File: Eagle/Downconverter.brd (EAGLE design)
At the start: 160 x 100 mm, 25 parts, among them J2 3.5HEADPHONEJACK, J5 U.FL_CONN, J6 U.FL_CONN, U1 5V_REG, U2 MIXER, U3 DUAL_OP_AMP_LMV822, U4 DIGITAL_POTDIGITAL_POT

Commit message: changes to layout
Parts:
- moved C1 1.80 mm to (3.17, 19.1)
- moved U1 1.42 mm to (10.2, 20.3)
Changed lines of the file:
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@@
 </autorouter>
 <elements>
-<element name="C1" library="764Library" package="R0603" package3d_urn="urn:adsk.eagle:package:26057/1" value="10uF" x="4.445" y="17.78" smashed="yes">
-<attribute name="NAME" x="3.81" y="18.415" size="1.27" layer="25"/>
-<attribute name="VALUE" x="2.54" y="15.875" size="1.27" layer="27"/>
+<element name="C1" library="764Library" package="R0603" package3d_urn="urn:adsk.eagle:package:26057/1" value="10uF" x="3.175" y="19.05" smashed="yes">
+<attribute name="NAME" x="1.27" y="16.51" size="1.27" layer="25"/>
+<attribute name="VALUE" x="1.27" y="15.24" size="1.27" layer="27"/>
 </element>
 <element name="C2" library="764Library" package="R0603" package3d_urn="urn:adsk.eagle:package:26057/1" value="100uF" x="-35.56" y="40.64" smashed="yes">
@@
 <attribute name="VALUE" x="-33.655" y="52.705" size="1.27" layer="27"/>
 </element>
-<element name="U1" library="764Library" package="5V_REG" value="5V_REG" x="11.43" y="19.685" smashed="yes" rot="R270">
-<attribute name="NAME" x="10.47" y="24.085" size="1.27" layer="25"/>
+<element name="U1" library="764Library" package="5V_REG" value="5V_REG" x="10.16" y="20.32" smashed="yes" rot="R270">
+<attribute name="NAME" x="9.2" y="24.72" size="1.27" layer="25"/>
 </element>
 <element name="U2" library="764Library" package="MIXER" value="MIXER" x="8.89" y="6.35" smashed="yes">
@@
 <wire x1="2.54" y1="8.685" x2="2.54" y2="5.285" width="0" layer="19" extent="1-1"/>
 <wire x1="2.54" y1="11.635" x2="2.54" y2="8.685" width="0" layer="19" extent="1-1"/>
-<wire x1="5.295" y1="17.78" x2="2.54" y2="11.635" width="0" layer="19" extent="1-1"/>
-<wire x1="2.54" y1="24.13" x2="5.295" y2="17.78" width="0" layer="19" extent="1-1"/>
+<wire x1="4.025" y1="19.05" x2="2.54" y2="11.635" width="0" layer="19" extent="1-1"/>
+<wire x1="2.54" y1="24.13" x2="4.025" y2="19.05" width="0" layer="19" extent="1-1"/>
 <wire x1="5.08" y1="26.67" x2="2.54" y2="24.13" width="0" layer="19" extent="1-1"/>
 <wire x1="-16.93" y1="49.53" x2="5.08" y2="26.67" width="0" layer="19" extent="1-1"/>
@@
 <contactref element="U1" pad="3"/>
 <contactref element="C1" pad="1"/>
-<wire x1="3.595" y1="17.78" x2="2.54" y2="21.59" width="0" layer="19" extent="1-1"/>
-<wire x1="8.305" y1="17.385" x2="3.595" y2="17.78" width="0" layer="19" extent="1-1"/>
+<wire x1="2.325" y1="19.05" x2="2.54" y2="21.59" width="0" layer="19" extent="1-1"/>
+<wire x1="7.035" y1="18.02" x2="2.325" y2="19.05" width="0" layer="19" extent="1-1"/>
 </signal>
 <signal name="N$1">
@@
 <contactref element="R2" pad="1"/>
 <wire x1="-22.44" y1="54.61" x2="-15.66" y2="54.61" width="0" layer="19" extent="1-1"/>
-<wire x1="8.305" y1="21.985" x2="-15.66" y2="54.61" width="0" layer="19" extent="1-1"/>
+<wire x1="7.035" y1="22.62" x2="-15.66" y2="54.61" width="0" layer="19" extent="1-1"/>
 </signal>
 <signal name="5V">
@@
 <contactref element="J7" pad="7"/>
 <wire x1="23.495" y1="26.67" x2="39.2938" y2="12.7" width="0" layer="19" extent="1-1"/>
-<wire x1="14.555" y1="19.685" x2="23.495" y2="26.67" width="0" layer="19" extent="1-1"/>
-<wire x1="8.305" y1="19.685" x2="14.555" y2="19.685" width="0" layer="19" extent="1-1"/>
-<wire x1="7.62" y1="26.67" x2="8.305" y2="19.685" width="0" layer="19" extent="1-1"/>
+<wire x1="13.285" y1="20.32" x2="23.495" y2="26.67" width="0" layer="19" extent="1-1"/>
+<wire x1="7.035" y1="20.32" x2="13.285" y2="20.32" width="0" layer="19" extent="1-1"/>
+<wire x1="7.62" y1="26.67" x2="7.035" y2="20.32" width="0" layer="19" extent="1-1"/>
 <wire x1="-20.74" y1="54.61" x2="7.62" y2="26.67" width="0" layer="19" extent="1-1"/>
 <wire x1="-36.41" y1="40.64" x2="-20.74" y2="54.61" width="0" layer="19" extent="1-1"/>

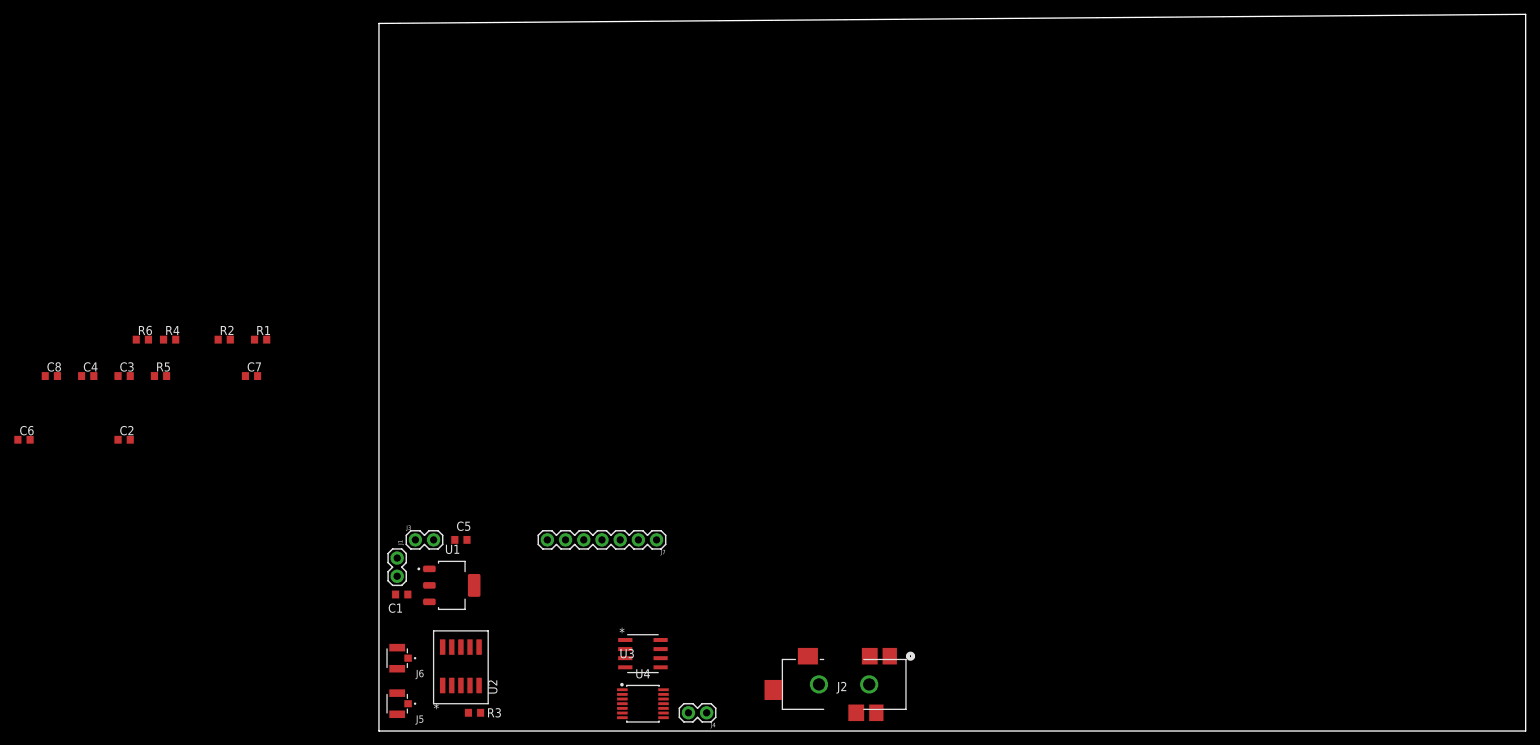
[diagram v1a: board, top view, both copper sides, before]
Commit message: Fixed SSCPW for Mixer
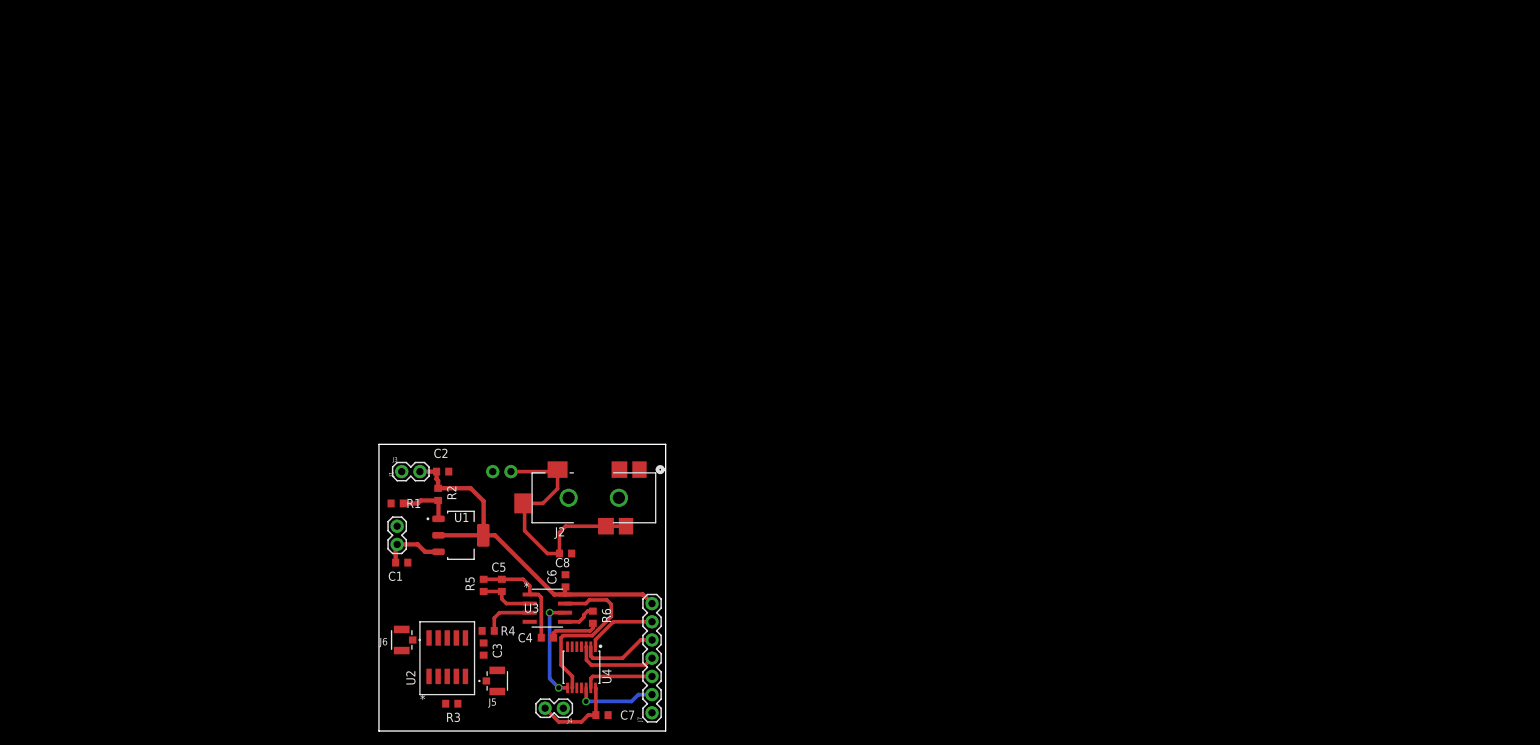
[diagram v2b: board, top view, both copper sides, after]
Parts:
- added J8: (no value), SparkFun-Connectors:1X02
- moved C6 78.1 mm to (26.0, 21.0), turned to 90 degrees
- moved C8 75.9 mm to (26.0, 24.8), turned to 180 degrees
- moved R6 73.8 mm to (29.8, 15.9), turned to 270 degrees
- moved C4 73.8 mm to (23.5, 13.0)
- moved C7 68.0 mm to (31.1, 2.22)
- moved C3 63.0 mm to (14.6, 11.4), turned to 90 degrees
- moved R4 60.2 mm to (15.2, 14.0), turned to 180 degrees
- moved R5 53.7 mm to (14.6, 20.3), turned to 270 degrees
- moved C2 44.7 mm to (8.89, 36.2)
- moved J2 43.6 mm to (28.6, 28.6)
- moved R2 36.8 mm to (8.26, 33.0), turned to 90 degrees
- moved R1 29.8 mm to (2.54, 31.8)
- moved J7 24.1 mm to (38.1, 2.54), turned to 90 degrees
- moved J4 20.0 mm to (25.7, 3.17)
- moved U3 14.8 mm to (23.5, 17.1)
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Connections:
- removed net N$9: C8.2, J2.3, J2.4, J2.7, J2.8
- new net RDR_OUT: C8.2, J2.3, J2.4, J2.7, J2.8, J8.1
- net GND: now also J8.2
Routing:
- net 5V: track 0.00 -> 50.8 mm
- net RDR_OUT: track 0.00 -> 37.4 mm
- net N$12: track 0.00 -> 24.5 mm
- net N$6: track 0.00 -> 15.4 mm
- net N$13: track 0.00 -> 14.4 mm, vias 0 -> 2
- net 3.3V: track 0.00 -> 12.5 mm
- net SDI: track 0.00 -> 11.7 mm
- net SHDN: track 0.00 -> 11.5 mm, vias 0 -> 1
- net SCK: track 0.00 -> 11.1 mm
- net SDO: track 0.00 -> 9.98 mm
- net CS: track 0.00 -> 9.91 mm
- net 9V: track 0.00 -> 8.82 mm
- net N$5: track 0.00 -> 7.74 mm
- net N$1: track 0.00 -> 7.62 mm
- net N$7: track 0.00 -> 7.32 mm
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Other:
- board size 160 x 100 mm -> 40 x 40 mm
